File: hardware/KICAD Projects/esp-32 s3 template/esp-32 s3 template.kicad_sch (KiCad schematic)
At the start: 28 parts, among them J1 TYPE-C-31-M-12, J2 TFTLCDS2, SW1 PTS810_SJM_250_SMTR_LFS, SW2 PTS810_SJM_250_SMTR_LFS, U1 AMS1117-3.3, U2 ESP32-S3-WROOM-1

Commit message: started the can integration
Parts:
- added C11: 10uF/16V, tantalum A, symbol CAN Integration-altium-import:root_0_Cap_Tantalum_adafruit.IntLib
- added C12, C15: ${ALTIUM_VALUE}, C0603, symbol CAN Integration-altium-import:root_2_Cap_0603_adafruit.IntLib
- added C13, C14: ${ALTIUM_VALUE}, C0603, symbol CAN Integration-altium-import:root_3_Cap_0603_adafruit.IntLib
- added J3: CAN to outer connector, Connector_Wire:SolderWire-0.1sqmm_1x04_P3.6mm_D0.4mm_OD1mm, symbol Connector_Generic:Conn_01x04
- added J5: Conn_01x02, Connector_Wire:SolderWire-0.75sqmm_1x02_P4.8mm_D1.25mm_OD2.3mm, symbol Connector_Generic:Conn_01x02
- added Jx: Conn_01x06, symbol Connector_Generic:Conn_01x06
- added POW1: RED LED, CHIPLED_0603, symbol CAN Integration-altium-import:root_0_LEDCHIP-LED0603_adafruit.IntLib
- added R7: ${ALTIUM_VALUE}, R0603, symbol CAN Integration-altium-import:root_1_Res_0603_adafruit.IntLib
- added R8: ${ALTIUM_VALUE}, R0603, symbol CAN Integration-altium-import:root_0_Res_0603_adafruit.IntLib
- added U3: MCP2515-I, SOIC-18_L11.6-W7.5-P1.27-LS10.3-BL, symbol CAN Integration-altium-import:root_0_MCP2515_adafruit.SCHLIB
- added U4: TJA1050DRG, SOIC-8E, symbol CAN Integration-altium-import:root_0_TJA1050DRG_adafruit.SCHLIB
- added U5: ~, 0_Custom:MLX90614, symbol 0_Custom:MLX90614
- added X1: ${ALTIUM_VALUE}, HC-49US_L11.5-W4.5-P4.88, symbol CAN Integration-altium-import:root_0_CRYSTAL-ECS-100-20-5PVX_adafruit.IntLib
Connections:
- net SCK: now reaches U2.6 (IO6)
- net GND renamed 0
- net 0: now also J5.2 (Pin_2), U5.4 (VSS)
- new net +3V: U5.3 (VDD)
- new net +5V: J5.1 (Pin_1)
- new net High: J3.2 (Pin_2), J3.4 (Pin_4)
- new net Low: J3.1 (Pin_1), J3.3 (Pin_3)
- new net SCL: U5.1 (SCL/Vz)
- new net SDA: U5.2 (SDA/PWM)
- no-connect marks 30 -> 37
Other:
- note added: "+5v"
- note added: "100nF"
- note added: "10K"
- note added: "10uF/16V"
- note added: "1K"
- note added: "22pF"
- note added: "8MHz"
- note added: "CAN Controller"
- note added: "CAN Transiver"
- note added: "Connector Pinout"
- note added: "GND"
- note added: "High"
- note added: "I/O"
- note added: "Low"
- note added: "SPI MODES: 0,0 & 1,1"
- note added: "Standardize later"
- note added: "Temp Sensor"
- note added: "Temperature Range: -40*C to +85*C"
- note added: "VIN: 2.7V-5.5V."
- note added: "mlx90614"
- moved on the sheet: C1, C10, C2, C3, C4, C5, C6, C7, C8, C9, D1, D2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

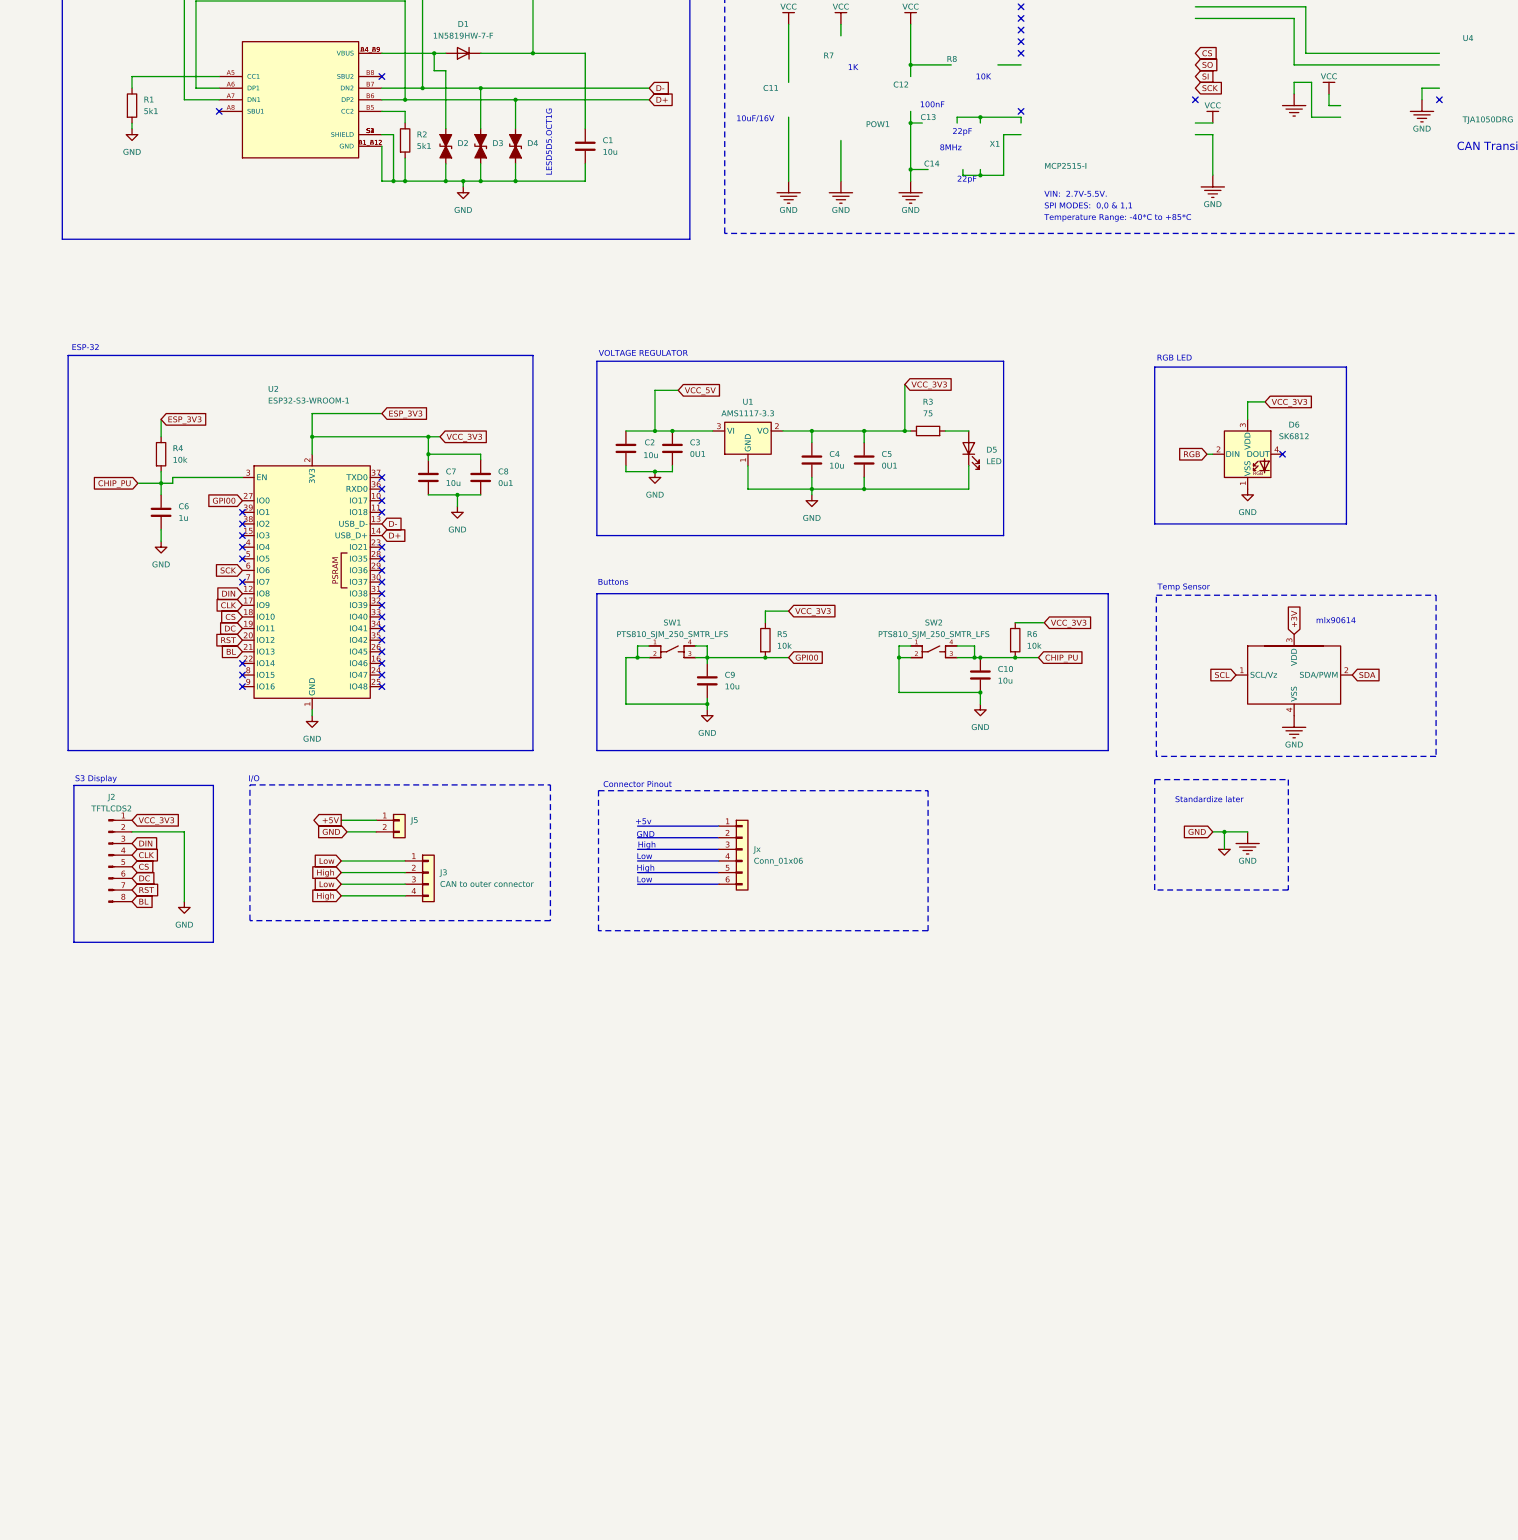
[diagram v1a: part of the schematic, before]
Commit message: completed s3 schem
didnt assign footprints yet tho
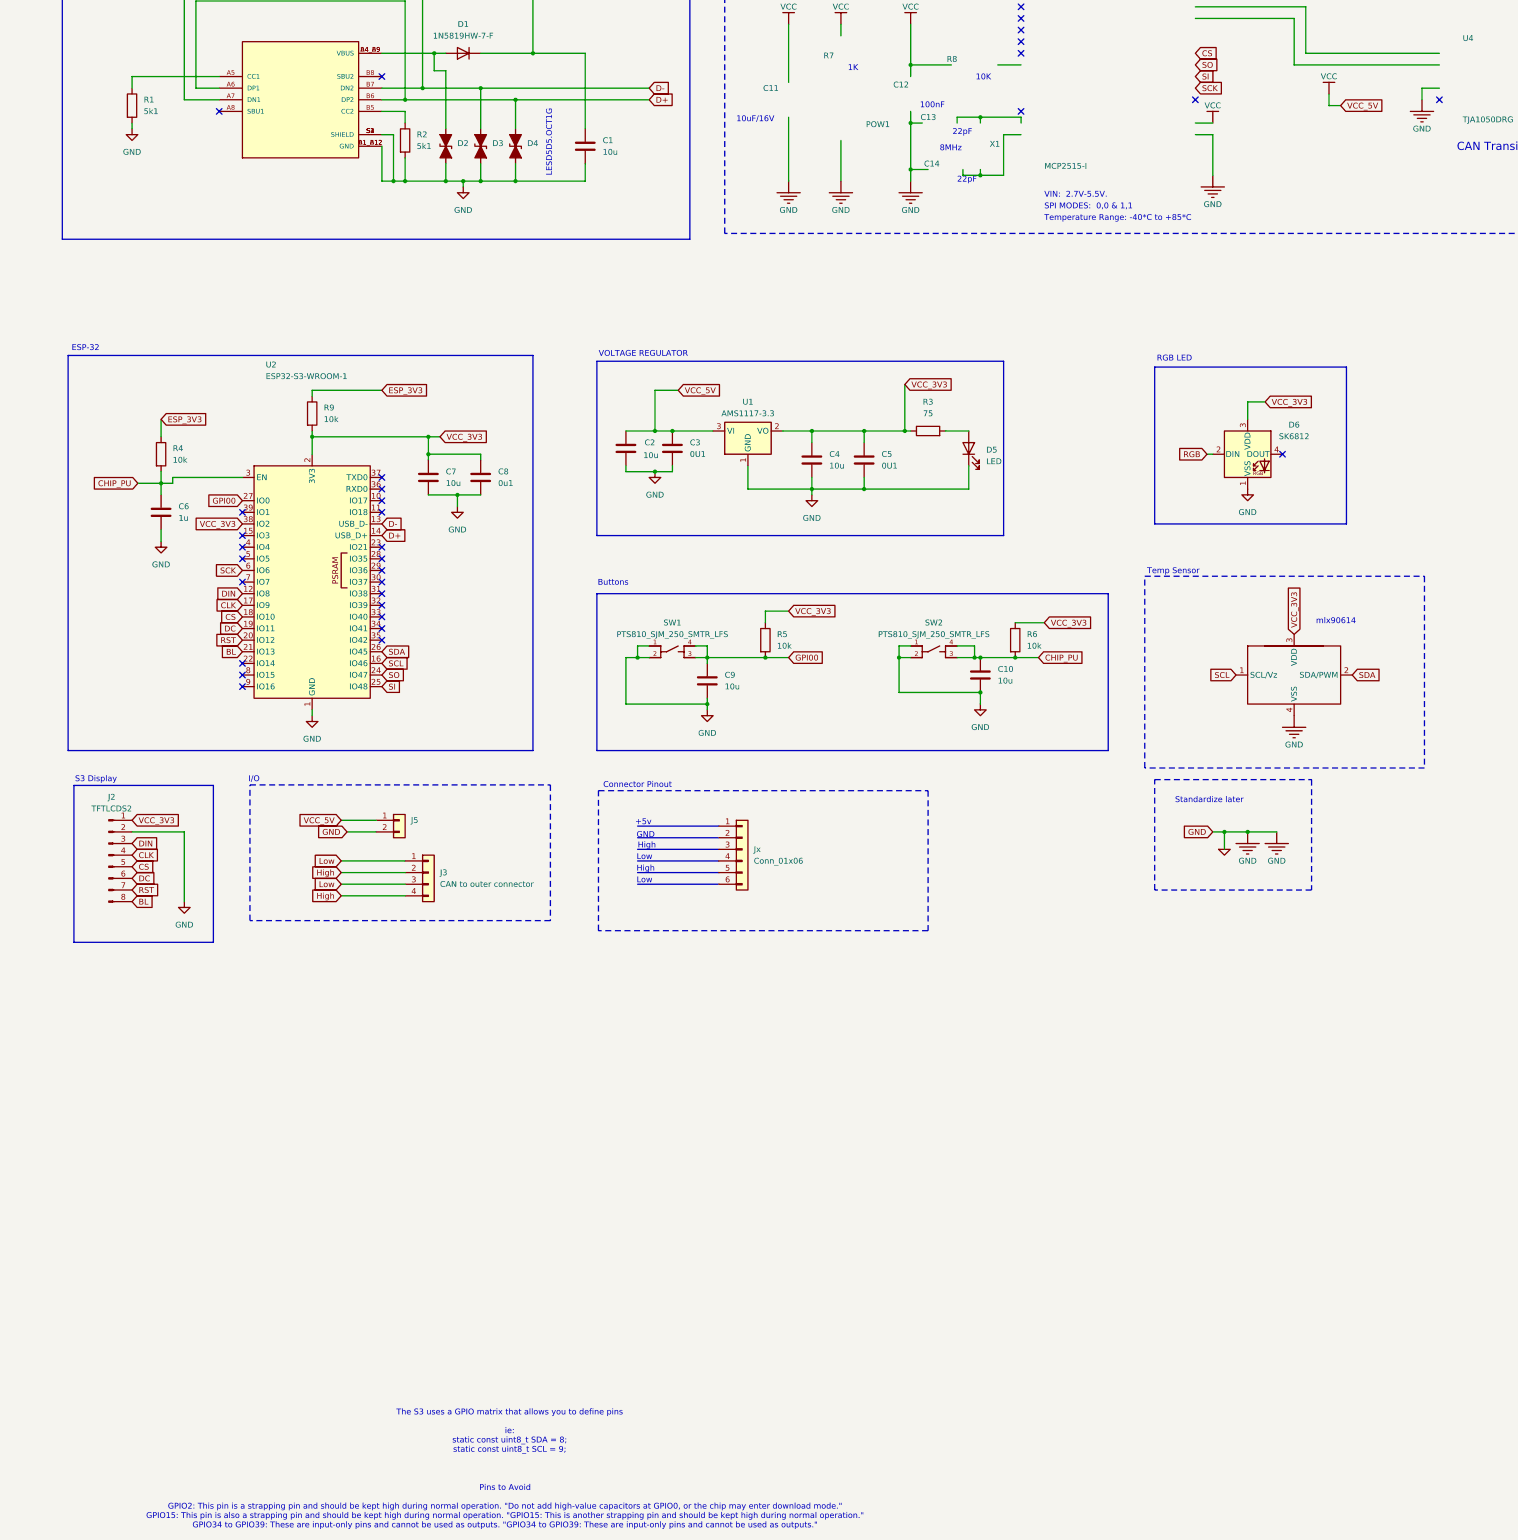
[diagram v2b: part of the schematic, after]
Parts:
- added R9: 10k, Resistor_SMD:R_0603_1608Metric, symbol Device:R
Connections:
- net +3V is gone; now on net VCC_3V3: U5.3 (VDD)
- net +5V is gone; now on net VCC: J5.1 (Pin_1)
- net VCC_5V is gone; now on net VCC: C1.1, C2.1, C3.1, D1.1 (K), U1.3 (VI)
- net ESP_3V3: now also R9.1; no longer C4.1, C5.1, C7.1, C8.1, D6.3 (VDD), J2.1 (Pin_1), R3.1, R5.1, R6.1, U1.2 (VO), U2.2 (3V3)
- net SCL: now also U2.16 (IO46)
- net SDA: now also U2.26 (IO45)
- net SI: now also U2.25 (IO48)
- net SO: now also U2.24 (IO47)
- net VCC_3V3: now reaches U2.38 (IO2)
- net VCC_3V3: now also C4.1, C5.1, C7.1, C8.1, D6.3 (VDD), J2.1 (Pin_1), R3.1, R5.1, R6.1, U1.2 (VO), U2.2 (3V3), R9.2
- no-connect marks 37 -> 32
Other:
- note added: "Pins to Avoid GPIO2: This pin is a strapping pin and should be kept high during normal operation. "Do not add high-value capacitors at GPIO0, or the chip may enter download mode." GPIO15: This pin is also a strapping pin and should be kept high during normal operation. "GPIO15: This is another strapping pin and should be kept high during normal operation." GPIO34 to GPIO39: These are input-only p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"
- note added: "The S3 uses a GPIO matrix that allows you to define pins ie: static const uint8_t SDA = 8; static const uint8_t SCL = 9;"

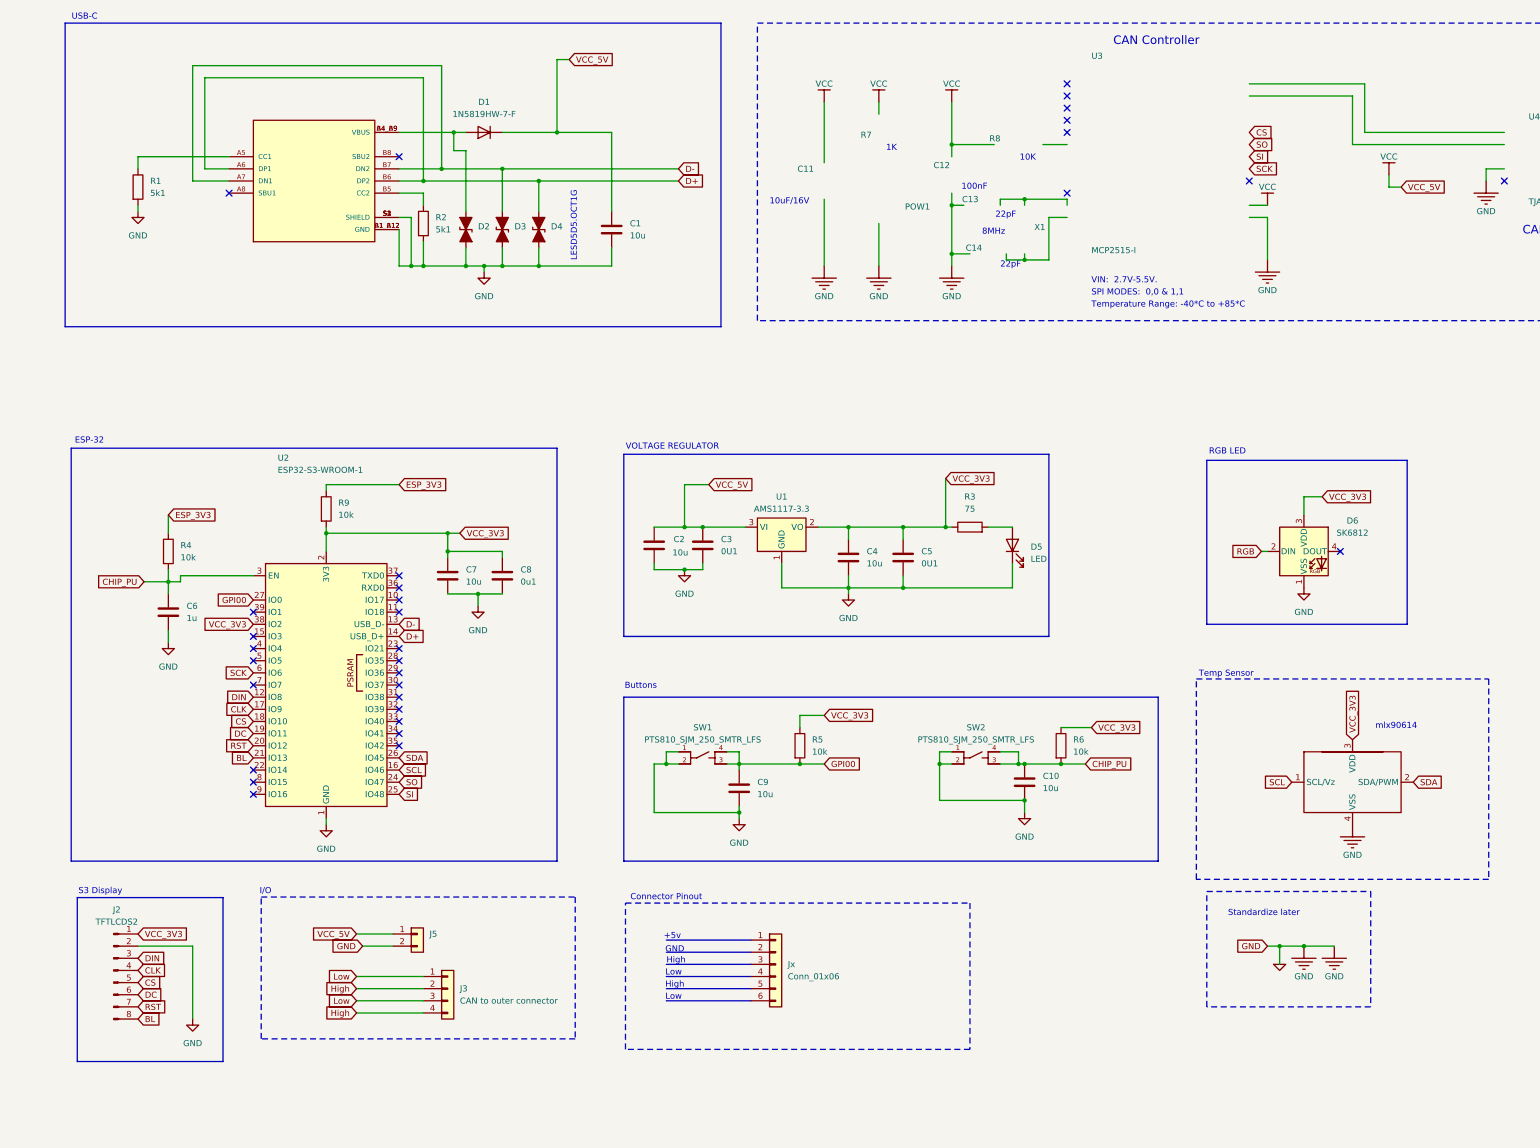
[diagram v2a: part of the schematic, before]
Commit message: finished pcb component layout for smd temp sense
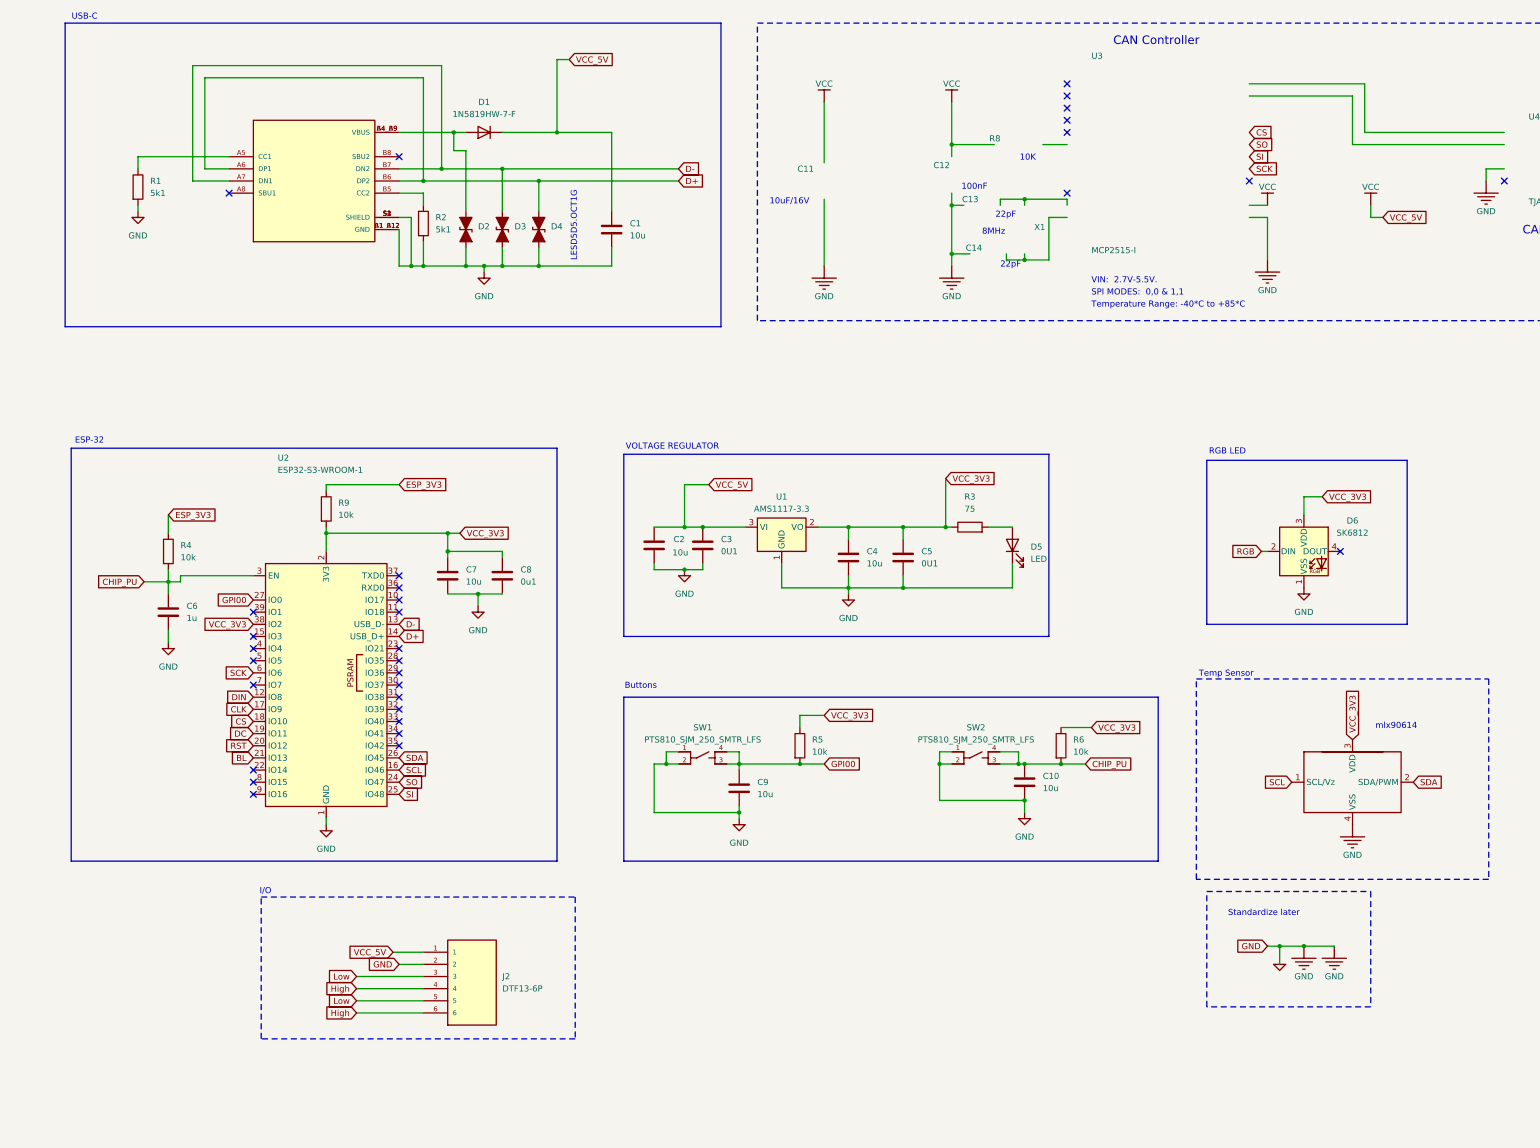
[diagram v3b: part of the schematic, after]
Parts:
- removed J2: TFTLCDS2, Connector_PinSocket_1.00mm:PinSocket_1x08_P1.00mm_Vertical, symbol Connector:Conn_01x08_Pin
- removed J3: CAN to outer connector, Connector_Wire:SolderWire-0.1sqmm_1x04_P3.6mm_D0.4mm_OD1mm, symbol Connector_Generic:Conn_01x04
- removed J5: Conn_01x02, Connector_Wire:SolderWire-0.75sqmm_1x02_P4.8mm_D1.25mm_OD2.3mm, symbol Connector_Generic:Conn_01x02
- removed Jx: Conn_01x06, symbol Connector_Generic:Conn_01x06
- removed POW1: RED LED, CHIPLED_0603, symbol CAN Integration-altium-import:root_0_LEDCHIP-LED0603_adafruit.IntLib
- removed R7: ${ALTIUM_VALUE}, R0603, symbol CAN Integration-altium-import:root_1_Res_0603_adafruit.IntLib
- added J2: DTF13-6P, 0_Custom:TE_DTF13-6P, symbol 0_Custom:DTF13-6P
- C11: footprint tantalum A -> Capacitor_Tantalum_SMD:CP_EIA-1608-08_AVX-J
- C12, C13, C14, C15: footprint C0603 -> Capacitor_SMD:C_0603_1608Metric
- R8: footprint R0603 -> Resistor_SMD:R_0603_1608Metric
- U3: footprint SOIC-18_L11.6-W7.5-P1.27-LS10.3-BL -> Package_SO:SOIC-18W_7.5x11.6mm_P1.27mm
- U4: footprint SOIC-8E -> Package_SO:SOIC-8_5.3x5.3mm_P1.27mm
- X1: footprint HC-49US_L11.5-W4.5-P4.88 -> Crystal:Crystal_SMD_HC49-SD
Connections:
- net 0: now also J2.2
- net High: now also J2.4, J2.6
- net Low: now also J2.3, J2.5
- net VCC: now also J2.1
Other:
- note removed: "+5v"
- note removed: "1K"
- note removed: "Connector Pinout"
- note removed: "GND"
- note removed: "High"
- note removed: "Low"
- note removed: "S3 Display"
